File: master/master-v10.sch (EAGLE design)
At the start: 44 parts, among them IC2 DS3231/SO, J1 AVR_SPI_PRG_6PTH, J2 TWIG-2.0-DIPD, J3 TWIG-2.0-DIPD, J4 TWIG-2.0-DIPD, U1 MCP9804, U2 ATMEGA640/1280/2560-A, U3 FT232RL-BASICSSOP, U4 AP1117E, U5 USD-SOCKETNEW, U6 INA169

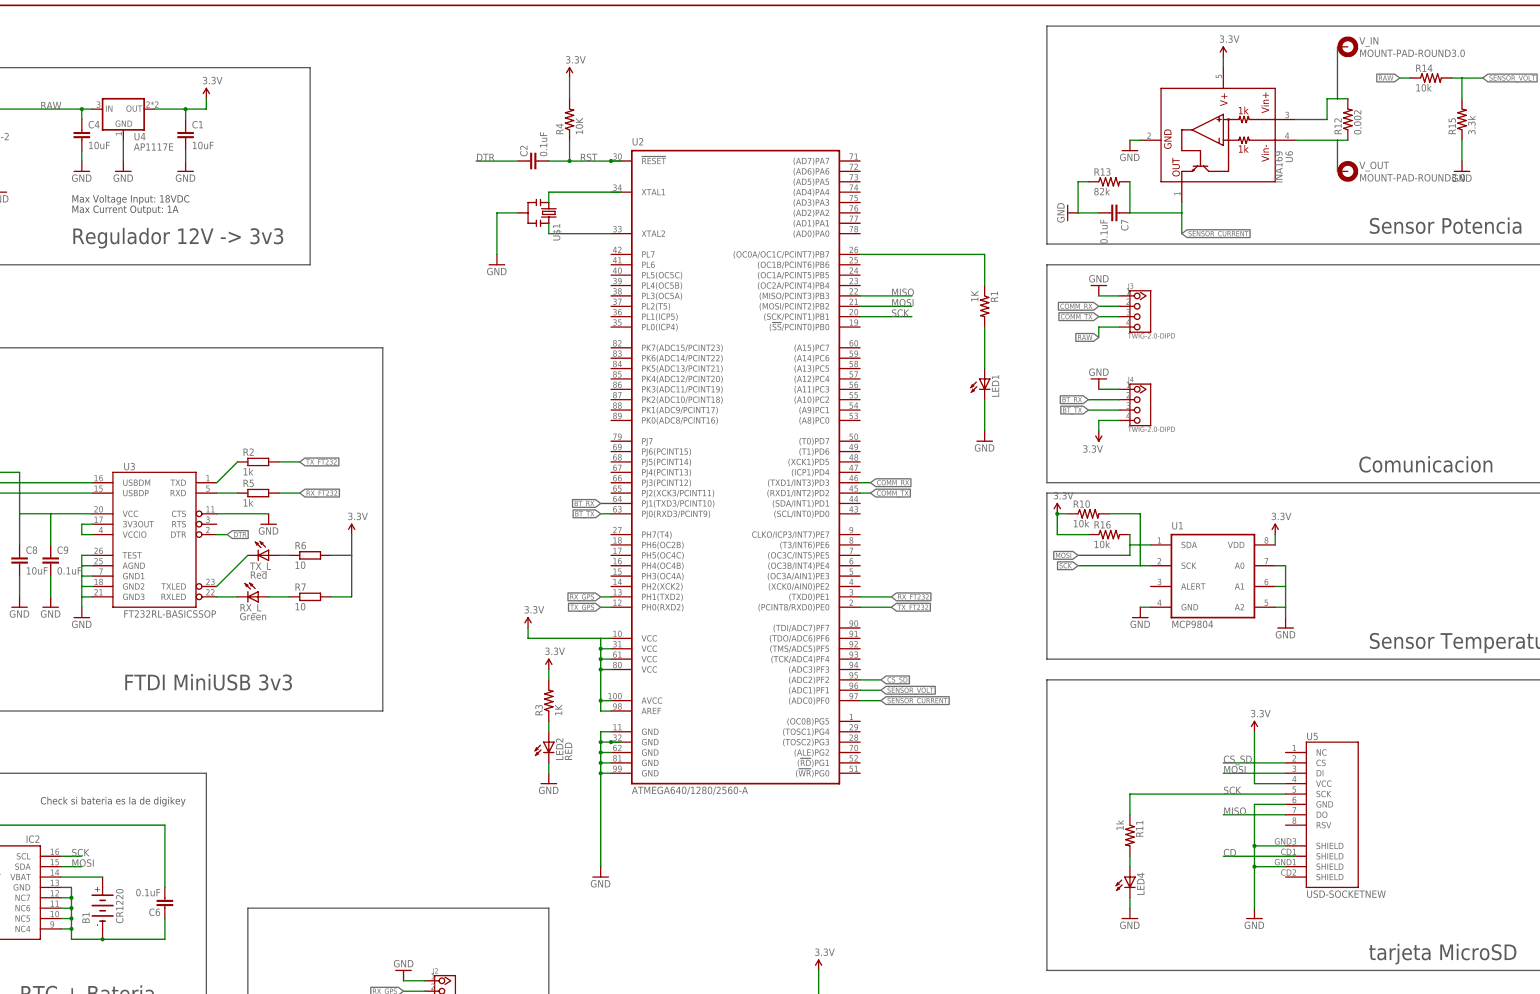
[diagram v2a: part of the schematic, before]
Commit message: actualizado brd, y arreglado tamaño de algunos componentes
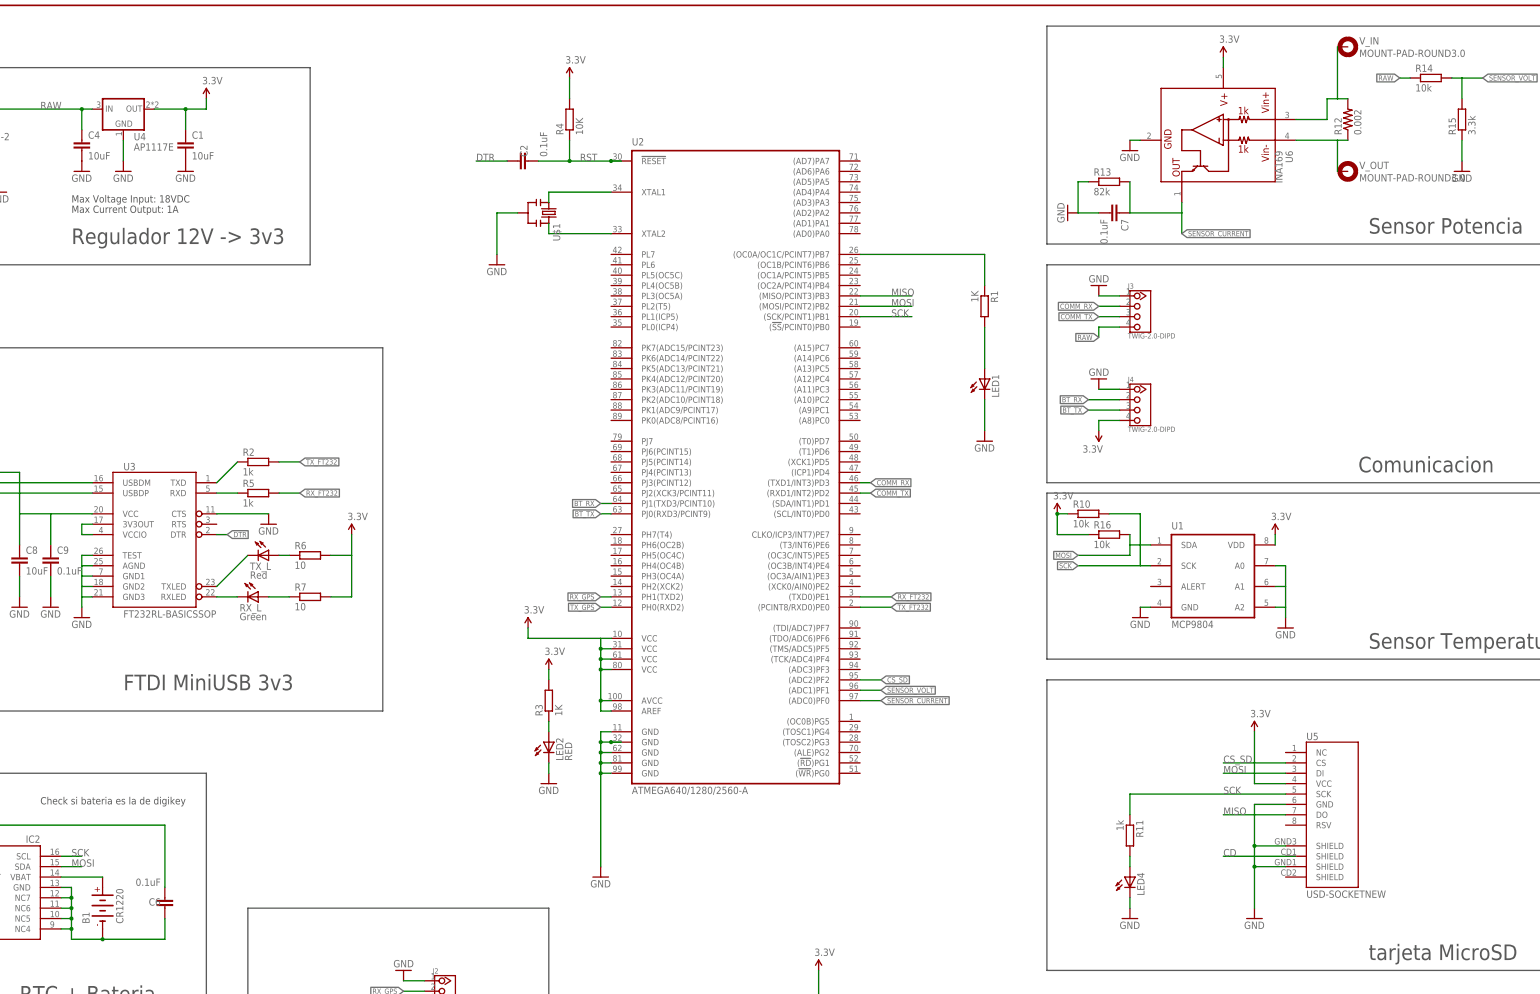
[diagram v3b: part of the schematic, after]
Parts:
- C1, C2, C4, C6, C7: device SparkFun:CAP0402-CAP -> rcl:C-EUC0805K
- R1, R10, R11, R13, R14, R15, R16, R3, R4: device SparkFun:RESISTOR0402-RES -> rcl:R-EU_R0805
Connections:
- removed net N$27: U1.A1
- net GND: now also U1.A1
- net N$2: now also U2.XTAL1
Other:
- moved on the sheet: C1, C2, C4
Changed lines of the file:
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@@
 <part name="GND25" library="SparkFun" deviceset="GND" device=""/>
 <part name="GND5" library="SparkFun" deviceset="GND" device=""/>
-<part name="C2" library="SparkFun" deviceset="CAP" device="0402-CAP" value="0.1uF"/>
-<part name="R1" library="SparkFun" deviceset="RESISTOR" device="0402-RES" value="1K"/>
+<part name="C2" library="rcl" deviceset="C-EU" device="C0805K" value="0.1uF"/>
+<part name="R1" library="rcl" deviceset="R-EU_" device="R0805" value="1K"/>
 <part name="GND2" library="SparkFun" deviceset="GND" device=""/>
-<part name="C1" library="SparkFun" deviceset="CAP" device="0402-CAP" value="10uF"/>
-<part name="C4" library="SparkFun" deviceset="CAP" device="0402-CAP" value="10uF"/>
+<part name="C1" library="rcl" deviceset="C-EU" device="C0805K" value="10uF"/>
+<part name="C4" library="rcl" deviceset="C-EU" device="C0805K" value="10uF"/>
 <part name="GND3" library="SparkFun" deviceset="GND" device=""/>
 <part name="GND6" library="SparkFun" deviceset="GND" device=""/>
-<part name="R3" library="SparkFun" deviceset="RESISTOR" device="0402-RES" value="1K"/>
+<part name="R3" library="rcl" deviceset="R-EU_" device="R0805" value="1K"/>
 <part name="IC2" library="adafruit" deviceset="DS3231" device="/SO"/>
 <part name="GND8" library="SparkFun" deviceset="GND" device=""/>
 <part name="U2" library="atmel-avr" deviceset="ATMEGA640/1280/2560" device="-A"/>
-<part name="R4" library="SparkFun" deviceset="RESISTOR" device="0402-RES" value="10K"/>
+<part name="R4" library="rcl" deviceset="R-EU_" device="R0805" value="10K"/>
 <part name="LED1" library="adafruit" deviceset="LED" device="CHIPLED_0805"/>
 <part name="LED2" library="adafruit" deviceset="LED" device="CHIPLED_0805" value="RED"/>
 <part name="B1" library="battery" deviceset="CR1220" device=""/>
-<part name="C6" library="SparkFun" deviceset="CAP" device="0402-CAP" value="0.1uF"/>
+<part name="C6" library="rcl" deviceset="C-EU" device="C0805K" value="0.1uF"/>
 <part name="GND1" library="SparkFun" deviceset="GND" device=""/>
 <part name="SUPPLY1" library="SparkFun-Aesthetics" deviceset="3.3V" device=""/>
@@
 <part name="U4" library="v-reg" deviceset="AP1117" device="E"/>
 <part name="GND18" library="SparkFun" deviceset="GND" device=""/>
-<part name="R10" library="SparkFun" deviceset="RESISTOR" device="0402-RES" value="10k"/>
+<part name="R10" library="rcl" deviceset="R-EU_" device="R0805" value="10k"/>
 <part name="GND19" library="SparkFun" deviceset="GND" device=""/>
 <part name="SUPPLY12" library="SparkFun-Aesthetics" deviceset="3.3V" device=""/>
 <part name="U5" library="SparkFun-Connectors" deviceset="USD-SOCKET" device="NEW"/>
 <part name="SUPPLY13" library="SparkFun-Aesthetics" deviceset="3.3V" device=""/>
-<part name="R11" library="SparkFun" deviceset="RESISTOR" device="0402-RES" value="1k"/>
+<part name="R11" library="rcl" deviceset="R-EU_" device="R0805" value="1k"/>
 <part name="LED4" library="adafruit" deviceset="LED" device="CHIPLED_0805"/>
 <part name="GND20" library="SparkFun" deviceset="GND" device=""/>
@@
 <part name="R12" library="SparkFun-Resistors" deviceset="RESISTOR" device="1206" value="0.002"/>
 <part name="U6" library="SparkFun-AnalogIC" deviceset="INA169" device=""/>
-<part name="R13" library="SparkFun" deviceset="RESISTOR" device="0402-RES" value="82k"/>
-<part name="C7" library="SparkFun" deviceset="CAP" device="0402-CAP" value="0.1uF"/>
+<part name="R13" library="rcl" deviceset="R-EU_" device="R0805" value="82k"/>
+<part name="C7" library="rcl" deviceset="C-EU" device="C0805K" value="0.1uF"/>
 <part name="GND4" library="SparkFun" deviceset="GND" device=""/>
-<part name="R14" library="SparkFun" deviceset="RESISTOR" device="0402-RES" value="10k"/>
-<part name="R15" library="SparkFun" deviceset="RESISTOR" device="0402-RES" value="3.3k"/>
+<part name="R14" library="rcl" deviceset="R-EU_" device="R0805" value="10k"/>
+<part name="R15" library="rcl" deviceset="R-EU_" device="R0805" value="3.3k"/>
 <part name="GND22" library="SparkFun" deviceset="GND" device=""/>
 <part name="U1" library="MCP9804" deviceset="MCP9804" device=""/>
 <part name="GND23" library="SparkFun" deviceset="GND" device=""/>
-<part name="R16" library="SparkFun" deviceset="RESISTOR" device="0402-RES" value="10k"/>
+<part name="R16" library="rcl" deviceset="R-EU_" device="R0805" value="10k"/>
 <part name="SUPPLY8" library="SparkFun-Aesthetics" deviceset="3.3V" device=""/>
 <part name="J2" library="Grove " deviceset="TWIG-2.0-DIP" device="D"/>
@@
 <instance part="LED2" gate="G$1" x="160.02" y="99.06"/>
 <instance part="B1" gate="G$1" x="50.8" y="58.42" rot="R90"/>
-<instance part="C6" gate="G$1" x="66.04" y="58.42" smashed="yes">
-<attribute name="NAME" x="65.024" y="58.293" size="1.778" layer="95" rot="R180"/>
-<attribute name="VALUE" x="65.024" y="63.119" size="1.778" layer="96" rot="R180"/>
+<instance part="C6" gate="G$1" x="66.04" y="60.96" smashed="yes">
+<attribute name="NAME" x="65.024" y="60.833" size="1.778" layer="95" rot="R180"/>
+<attribute name="VALUE" x="65.024" y="65.659" size="1.778" layer="96" rot="R180"/>
 </instance>
 <instance part="GND1" gate="1" x="302.26" y="243.84"/>
@@
 <instance part="U6" gate="G$1" x="322.58" y="246.38" rot="R270"/>
 <instance part="R13" gate="G$1" x="297.18" y="236.22"/>
-<instance part="C7" gate="G$1" x="297.18" y="228.6" rot="R270"/>
+<instance part="C7" gate="G$1" x="299.72" y="228.6" rot="R270"/>
 <instance part="GND4" gate="1" x="287.02" y="228.6" rot="R270"/>
 <instance part="R14" gate="G$1" x="375.92" y="261.62"/>
@@
 <net name="GND" class="1">
 <segment>
-<wire x1="71.12" y1="241.3" x2="71.12" y2="243.84" width="0.1524" layer="91"/>
 <pinref part="GND25" gate="1" pin="GND"/>
 <pinref part="C1" gate="G$1" pin="2"/>
@@
 <pinref part="C4" gate="G$1" pin="2"/>
 <pinref part="GND3" gate="1" pin="GND"/>
-<wire x1="45.72" y1="243.84" x2="45.72" y2="241.3" width="0.1524" layer="91"/>
 </segment>
 <segment>
@@
 </segment>
 <segment>
+<pinref part="U1" gate="G$1" pin="A2"/>
+<wire x1="337.82" y1="132.08" x2="340.36" y2="132.08" width="0.1524" layer="91"/>
+<wire x1="340.36" y1="132.08" x2="340.36" y2="129.54" width="0.1524" layer="91"/>
+<pinref part="GND23" gate="1" pin="GND"/>
 <pinref part="U1" gate="G$1" pin="A0"/>
 <wire x1="337.82" y1="142.24" x2="340.36" y2="142.24" width="0.1524" layer="91"/>
-<pinref part="U1" gate="G$1" pin="A2"/>
-<wire x1="337.82" y1="132.08" x2="340.36" y2="132.08" width="0.1524" layer="91"/>
-<wire x1="340.36" y1="142.24" x2="340.36" y2="132.08" width="0.1524" layer="91"/>
-<wire x1="340.36" y1="132.08" x2="340.36" y2="129.54" width="0.1524" layer="91"/>
-<pinref part="GND23" gate="1" pin="GND"/>
+<pinref part="U1" gate="G$1" pin="A1"/>
+<wire x1="337.82" y1="137.16" x2="340.36" y2="137.16" width="0.1524" layer="91"/>
+<wire x1="340.36" y1="142.24" x2="340.36" y2="137.16" width="0.1524" layer="91"/>
+<wire x1="340.36" y1="137.16" x2="340.36" y2="132.08" width="0.1524" layer="91"/>
 </segment>
 <segment>
@@
 <pinref part="C4" gate="G$1" pin="1"/>
 <wire x1="45.72" y1="254" x2="48.26" y2="254" width="0.1524" layer="91"/>
-<wire x1="45.72" y1="251.46" x2="45.72" y2="254" width="0.1524" layer="91"/>
+<wire x1="45.72" y1="248.92" x2="45.72" y2="254" width="0.1524" layer="91"/>
 <junction x="45.72" y="254"/>
 <pinref part="U4" gate="G$1" pin="IN"/>
@@
 <net name="DTR" class="0">
 <segment>
-<wire x1="152.4" y1="241.3" x2="142.24" y2="241.3" width="0.1524" layer="91"/>
+<wire x1="149.86" y1="241.3" x2="142.24" y2="241.3" width="0.1524" layer="91"/>
 <label x="142.24" y="241.3" size="1.778" layer="95"/>
 <pinref part="C2" gate="G$1" pin="2"/>
@@
 <pinref part="R4" gate="G$1" pin="1"/>
 <pinref part="C2" gate="G$1" pin="1"/>
-<wire x1="165.1" y1="241.3" x2="160.02" y2="241.3" width="0.1524" layer="91"/>
+<wire x1="165.1" y1="241.3" x2="157.48" y2="241.3" width="0.1524" layer="91"/>
 <junction x="165.1" y="241.3"/>
 <pinref part="U2" gate="G$1" pin="!RESET!"/>
@@
 <wire x1="71.12" y1="254" x2="76.2" y2="254" width="0.1524" layer="91"/>
 <wire x1="76.2" y1="254" x2="76.2" y2="256.54" width="0.1524" layer="91"/>
-<wire x1="71.12" y1="254" x2="71.12" y2="251.46" width="0.1524" layer="91"/>
+<wire x1="71.12" y1="254" x2="71.12" y2="248.92" width="0.1524" layer="91"/>
 <pinref part="C1" gate="G$1" pin="1"/>
 <wire x1="71.12" y1="254" x2="63.5" y2="254" width="0.1524" layer="91"/>
@@
 </segment>
 </net>
-<net name="N$27" class="0">
-<segment>
-<pinref part="U1" gate="G$1" pin="A1"/>
-<wire x1="337.82" y1="137.16" x2="340.36" y2="137.16" width="0.1524" layer="91"/>
-</segment>
-</net>
 <net name="CS_SD" class="0">
 <segment>
@@
 <net name="N$2" class="0">
 <segment>
-<wire x1="177.8" y1="233.68" x2="160.02" y2="233.68" width="0.1524" layer="91"/>
 <wire x1="160.02" y1="233.68" x2="160.02" y2="231.14" width="0.1524" layer="91"/>
 <pinref part="U$1" gate="G$1" pin="1"/>
-</segment>
-</net>
+<pinref part="U2" gate="G$1" pin="XTAL1"/>
+<wire x1="160.02" y1="233.68" x2="175.26" y2="233.68" width="0.1524" layer="91"/>
+</segment>
+</net>

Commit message: orden en esquematico
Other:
- note added: "BLUETOOTH"
- note added: "Comunicación Banco"
- note removed: "Comunicacion"
- moved on the sheet: J3, J4
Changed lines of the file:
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@@
 <wire x1="281.94" y1="43.18" x2="281.94" y2="114.3" width="0.2032" layer="97"/>
 <text x="360.68" y="45.72" size="3.81" layer="97">tarjeta MicroSD</text>
-<wire x1="281.94" y1="215.9" x2="411.48" y2="215.9" width="0.2032" layer="97"/>
-<wire x1="411.48" y1="215.9" x2="411.48" y2="162.56" width="0.2032" layer="97"/>
-<wire x1="411.48" y1="162.56" x2="281.94" y2="162.56" width="0.2032" layer="97"/>
-<wire x1="281.94" y1="162.56" x2="281.94" y2="215.9" width="0.2032" layer="97"/>
-<text x="358.14" y="165.1" size="3.81" layer="97">Comunicacion</text>
+<wire x1="325.12" y1="215.9" x2="411.48" y2="215.9" width="0.2032" layer="97"/>
+<wire x1="411.48" y1="215.9" x2="411.48" y2="193.04" width="0.2032" layer="97"/>
+<wire x1="411.48" y1="193.04" x2="325.12" y2="193.04" width="0.2032" layer="97"/>
+<wire x1="325.12" y1="193.04" x2="325.12" y2="215.9" width="0.2032" layer="97"/>
+<text x="358.14" y="195.58" size="3.81" layer="97">Comunicación Banco</text>
 <wire x1="86.36" y1="58.42" x2="160.02" y2="58.42" width="0.1524" layer="97"/>
 <wire x1="160.02" y1="58.42" x2="160.02" y2="10.16" width="0.1524" layer="97"/>
@@
 <wire x1="86.36" y1="10.16" x2="86.36" y2="58.42" width="0.1524" layer="97"/>
 <text x="91.44" y="12.7" size="3.81" layer="97">GPS</text>
+<text x="373.38" y="167.64" size="3.81" layer="97">BLUETOOTH</text>
+<wire x1="411.48" y1="190.5" x2="337.82" y2="190.5" width="0.2032" layer="97"/>
+<wire x1="411.48" y1="165.1" x2="337.82" y2="165.1" width="0.2032" layer="97"/>
+<wire x1="337.82" y1="165.1" x2="337.82" y2="190.5" width="0.2032" layer="97"/>
+<wire x1="411.48" y1="190.5" x2="411.48" y2="165.1" width="0.2032" layer="97"/>
 </plain>
 <instances>
@@
 <instance part="GND24" gate="1" x="124.46" y="43.18" rot="R180"/>
 <instance part="SUPPLY14" gate="G$1" x="124.46" y="30.48" rot="R180"/>
-<instance part="J3" gate="G$1" x="303.53" y="204.47"/>
-<instance part="GND15" gate="1" x="294.64" y="210.82" rot="R180"/>
-<instance part="J4" gate="G$1" x="303.53" y="181.61"/>
-<instance part="GND16" gate="1" x="294.64" y="187.96" rot="R180"/>
-<instance part="SUPPLY10" gate="G$1" x="294.64" y="175.26" rot="R180"/>
+<instance part="J3" gate="G$1" x="349.25" y="204.47"/>
+<instance part="GND15" gate="1" x="340.36" y="210.82" rot="R180"/>
+<instance part="J4" gate="G$1" x="361.95" y="179.07"/>
+<instance part="GND16" gate="1" x="353.06" y="185.42" rot="R180"/>
+<instance part="SUPPLY10" gate="G$1" x="353.06" y="172.72" rot="R180"/>
 <instance part="U$1" gate="G$1" x="160.02" y="228.6" rot="R270"/>
 <instance part="JP2" gate="G$1" x="15.24" y="251.46"/>
@@
 <pinref part="J3" gate="G$1" pin="1"/>
 <pinref part="GND15" gate="1" pin="GND"/>
-<wire x1="294.64" y1="208.28" x2="299.72" y2="208.28" width="0.1524" layer="91"/>
+<wire x1="340.36" y1="208.28" x2="345.44" y2="208.28" width="0.1524" layer="91"/>
 </segment>
 <segment>
 <pinref part="J4" gate="G$1" pin="1"/>
 <pinref part="GND16" gate="1" pin="GND"/>
-<wire x1="294.64" y1="185.42" x2="299.72" y2="185.42" width="0.1524" layer="91"/>
+<wire x1="353.06" y1="182.88" x2="358.14" y2="182.88" width="0.1524" layer="91"/>
 </segment>
 <segment>
@@
 <segment>
 <pinref part="J3" gate="G$1" pin="4"/>
-<wire x1="299.72" y1="200.66" x2="294.64" y2="200.66" width="0.1524" layer="91"/>
-<wire x1="294.64" y1="200.66" x2="294.64" y2="198.12" width="0.1524" layer="91"/>
-<label x="294.64" y="198.12" size="1.27" layer="95" rot="R180" xref="yes"/>
+<wire x1="345.44" y1="200.66" x2="340.36" y2="200.66" width="0.1524" layer="91"/>
+<wire x1="340.36" y1="200.66" x2="340.36" y2="198.12" width="0.1524" layer="91"/>
+<label x="340.36" y="198.12" size="1.27" layer="95" rot="R180" xref="yes"/>
 </segment>
 </net>
@@
 <segment>
 <pinref part="J4" gate="G$1" pin="4"/>
-<wire x1="299.72" y1="177.8" x2="294.64" y2="177.8" width="0.1524" layer="91"/>
-<wire x1="294.64" y1="177.8" x2="294.64" y2="175.26" width="0.1524" layer="91"/>
+<wire x1="358.14" y1="175.26" x2="353.06" y2="175.26" width="0.1524" layer="91"/>
+<wire x1="353.06" y1="175.26" x2="353.06" y2="172.72" width="0.1524" layer="91"/>
 <pinref part="SUPPLY10" gate="G$1" pin="3.3V"/>
 </segment>
@@
 <segment>
 <pinref part="J4" gate="G$1" pin="2"/>
-<wire x1="299.72" y1="182.88" x2="292.1" y2="182.88" width="0.1524" layer="91"/>
-<label x="292.1" y="182.88" size="1.27" layer="95" rot="R180" xref="yes"/>
+<wire x1="358.14" y1="180.34" x2="350.52" y2="180.34" width="0.1524" layer="91"/>
+<label x="350.52" y="180.34" size="1.27" layer="95" rot="R180" xref="yes"/>
 </segment>
 </net>
@@
 <segment>
 <pinref part="J4" gate="G$1" pin="3"/>
-<wire x1="299.72" y1="180.34" x2="292.1" y2="180.34" width="0.1524" layer="91"/>
-<label x="292.1" y="180.34" size="1.27" layer="95" rot="R180" xref="yes"/>
+<wire x1="358.14" y1="177.8" x2="350.52" y2="177.8" width="0.1524" layer="91"/>
+<label x="350.52" y="177.8" size="1.27" layer="95" rot="R180" xref="yes"/>
 </segment>
 </net>
@@
 <segment>
 <pinref part="J3" gate="G$1" pin="2"/>
-<wire x1="299.72" y1="205.74" x2="294.64" y2="205.74" width="0.1524" layer="91"/>
-<label x="294.64" y="205.74" size="1.27" layer="95" rot="R180" xref="yes"/>
+<wire x1="345.44" y1="205.74" x2="340.36" y2="205.74" width="0.1524" layer="91"/>
+<label x="340.36" y="205.74" size="1.27" layer="95" rot="R180" xref="yes"/>
 </segment>
 <segment>
@@
 <segment>
 <pinref part="J3" gate="G$1" pin="3"/>
-<wire x1="299.72" y1="203.2" x2="294.64" y2="203.2" width="0.1524" layer="91"/>
-<label x="294.64" y="203.2" size="1.27" layer="95" rot="R180" xref="yes"/>
-</segment>
-<segment>
+<wire x1="345.44" y1="203.2" x2="340.36" y2="203.2" width="0.1524" layer="91"/>
+<label x="340.36" y="203.2" size="1.27" layer="95" rot="R180" xref="yes"/>
+</segment>
+<segment>

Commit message: more traces
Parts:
- renumbered B1 to BAT, IC2 to RTC, J1 to ISP, J2 to GPS, J3 to BANCO, J4 to BLE, RX_L to RX, TX_L to TX, U1 to TEMP, U2 to ATMEGA1280, U3 to FTDI, U4 to 3V3, U5 to MICROSD, U6 to INA169
